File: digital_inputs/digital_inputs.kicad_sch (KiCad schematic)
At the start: 130 parts, among them J1 6437288-2, J10 Conn_01x01, J11 Conn_01x01, J12 Conn_01x01, J13 Conn_01x01, J14 Conn_01x01, J15 Conn_01x01, J16 Conn_01x01, J17 Conn_01x01, J19 6437288-3, J3 Conn_01x08, J4 Conn_01x01, J5 Conn_01x02, J6 Conn_01x04, J7 Conn_01x04, J8 Conn_01x04, J9 Conn_01x04, Q1 AO3400A, Q2 AO3400A, Q3 AO3400A, Q4 AO3400A, Q5 AO3400A, Q6 AO3400A, Q7 AO3400A, Q8 AO3400A, U1 OPA4192IPW, U10 ULN2003A, U11 NUCLEO-F429ZI, U12 TJA1051T-3, U2 CD4067BM96, U3 CD4067BM96, U4 CD4067BM96, U5 CD4067BM96, U6 CD4067BM96, U7 CD4067BM96, U8 TC4427, U9 TC4427

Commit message: Upd pcb
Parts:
- removed U11: NUCLEO-F429ZI, lib:MODULE_NUCLEO-F429ZI, symbol NUCLEO-F429ZI:NUCLEO-F429ZI
- added D2: PESD1CAN, Package_TO_SOT_SMD:SOT-23, symbol semiconductors:PESD1CAN
- added H1, H2, H3, H4, H5: MountingHole, MountingHole:MountingHole_3.2mm_M3, symbol Mechanical:MountingHole
- added J18: Conn_02x05_Odd_Even, Connector_PinHeader_2.54mm:PinHeader_2x05_P2.54mm_Vertical, symbol Connector_Generic:Conn_02x05_Odd_Even
- added J2: Conn_02x07_Odd_Even, Connector_PinHeader_2.54mm:PinHeader_2x07_P2.54mm_Vertical, symbol Connector_Generic:Conn_02x07_Odd_Even
- added J20: Conn_02x24_Odd_Even, Connector_PinHeader_2.54mm:PinHeader_2x24_P2.54mm_Vertical, symbol Connector_Generic:Conn_02x24_Odd_Even
- added J21: Conn_02x08_Odd_Even, Connector_PinHeader_2.54mm:PinHeader_2x08_P2.54mm_Vertical, symbol Connector_Generic:Conn_02x08_Odd_Even
- added J22: Conn_02x15_Odd_Even, Connector_PinHeader_2.54mm:PinHeader_2x15_P2.54mm_Vertical, symbol Connector_Generic:Conn_02x15_Odd_Even
- added J23, J25: Conn_02x10_Odd_Even, Connector_PinHeader_2.54mm:PinHeader_2x10_P2.54mm_Vertical, symbol Connector_Generic:Conn_02x10_Odd_Even
- added J24: Conn_02x17_Odd_Even, Connector_PinHeader_2.54mm:PinHeader_2x17_P2.54mm_Vertical, symbol Connector_Generic:Conn_02x17_Odd_Even
- added J26: Conn_02x06_Odd_Even, Connector_PinHeader_2.54mm:PinHeader_2x06_P2.54mm_Vertical, symbol Connector_Generic:Conn_02x06_Odd_Even
- added J27: Conn_02x16_Odd_Even, Connector_PinHeader_2.54mm:PinHeader_2x16_P2.54mm_Vertical, symbol Connector_Generic:Conn_02x16_Odd_Even
- added J28: Conn_02x04_Odd_Even, Connector_PinHeader_2.54mm:PinHeader_2x04_P2.54mm_Vertical, symbol Connector_Generic:Conn_02x04_Odd_Even
- added R56: DNP, Resistor_SMD:R_0402_1005Metric, symbol hellen1-wbo-rescue:R-Device
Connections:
- net +12V: now also J18.10 (Pin_10)
- net +5V: now also J18.4 (Pin_4)
- net ADR0: now also J25.2 (Pin_2)
- net ADR1: now also J25.4 (Pin_4)
- net ADR2: now also J25.6 (Pin_6)
- net ADR3: now also J25.13 (Pin_13)
- net CAN_H: now also D2.1 (G), R56.1
- net CAN_L: now also D2.2 (D), R56.2
- net CAN_RX: now also J25.14 (Pin_14)
- net CAN_TX: now also J25.12 (Pin_12)
- net GND: now also D2.3 (S), J18.5 (Pin_5), J18.6 (Pin_6), J18.8 (Pin_8), J2.8 (Pin_8), J20.25 (Pin_25), J20.36 (Pin_36), J20.47 (Pin_47), J20.48 (Pin_48), J21.11 (Pin_11), J21.13 (Pin_13), J22.12 (Pin_12), J22.23 (Pin_23), J23.8 (Pin_8), J24.17 (Pin_17), J24.22 (Pin_22), J24.27 (Pin_27), J24.3 (Pin_3), J24.5 (Pin_5), J25.20 (Pin_20), J25.9 (Pin_9), J26.12 (Pin_12), J27.22 (Pin_22), J27.31 (Pin_31), J27.7 (Pin_7), J28.7 (Pin_7), J28.8 (Pin_8)
- net IN0: now also J27.6 (Pin_6)
- net IN1: now also J27.4 (Pin_4)
- net IN2: now also J27.26 (Pin_26)
- net IN3: now also J27.10 (Pin_10)
- net MUX_OFF: now also J25.15 (Pin_15)
- net OUT0: now also J25.16 (Pin_16)
- net OUT1: now also J25.18 (Pin_18)
- net OUT2: now also J25.19 (Pin_19)
- net OUT3: now also J27.2 (Pin_2)
- net +3V3 renamed +3.3V
- net +3.3V: now also J18.2 (Pin_2)
- net HALL0_0 renamed DIG_0
- net DIG_0: now also J27.32 (Pin_32)
- net HALL0_1 renamed DIG_1
- net DIG_1: now also J27.12 (Pin_12)
- net HALL0_2 renamed DIG_2
- net DIG_2: now also J27.8 (Pin_8)
- net HALL0_3 renamed DIG_3
- net DIG_3: now also J27.20 (Pin_20)
- net HALL0_4 renamed DIG_4
- net DIG_4: now also J27.15 (Pin_15)
- net HALL0_5 renamed DIG_5
- net DIG_5: now also J27.24 (Pin_24)
- net HALL0_6 renamed DIG_6
- net DIG_6: now also J27.17 (Pin_17)
- net HALL0_7 renamed DIG_7
- net DIG_7: now also J27.23 (Pin_23)
- net OUT_HALL0_0 renamed OUT_DIG_0
- net OUT_HALL0_1 renamed OUT_DIG_1
- net OUT_HALL0_2 renamed OUT_DIG_2
- net OUT_HALL0_3 renamed OUT_DIG_3
- net OUT_HALL0_4 renamed OUT_DIG_4
- net OUT_HALL0_5 renamed OUT_DIG_5
- net OUT_HALL0_6 renamed OUT_DIG_6
- net OUT_HALL0_7 renamed OUT_DIG_7
- no-connect marks 19 -> 220
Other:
- moved on the sheet: C11

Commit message: #14 #16 #23
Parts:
- R24, R30: value 910 -> 820; LCSC C23264 -> C23253
- R26, R32, R39, R49: value 470 -> 820; LCSC C23179 -> C23253
- R27: value 100 -> 120; LCSC C22775 -> C22787
- R28, R43, R54, R55: value 910 -> 470; LCSC C23264 -> C23179
- R29: value 330 -> 100
- R31: value 470 -> 220; LCSC C23179 -> C22962
- R34: value 100 -> 470; LCSC C22775 -> C23179
- R35: value 100 -> 220; LCSC C22775 -> C22962
- R36: value 330 -> 820; LCSC C23138 -> C23253
- R37, R58: value 330 -> 510; LCSC C23138 -> C23193
- R38: value 910 -> 510; LCSC C23264 -> C23193
- R42: value 330 -> 220; LCSC C23138 -> C22962
- R53: value 470 -> 330; LCSC C23179 -> C23138
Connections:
- net 5V_2: now also R38.1; no longer R39.1
- net GND: now also R39.2; no longer R38.2
- net REF12: now also R38.2, R39.1; no longer R38.1, R39.2
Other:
- note added: "0.6V"
- note added: "0.8V"
- note added: "1.1V"
- note added: "1.4V"
- note added: "1.6V"
- note added: "1.9V"
- note added: "3.1V"
- note added: "3.4V"
- note removed: "1.2V"
- note removed: "1.3V"
- note removed: "1.7V"
- note removed: "3.3V"
- note removed: "3.7V"

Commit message: check
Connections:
- net 5V_2: now also R39.1; no longer R38.1
- net GND: now also R38.1; no longer R39.2
- net REF12: now also R39.2; no longer R39.1
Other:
- moved on the sheet: R38, R39
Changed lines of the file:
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@@
     (stroke (width 0) (type default))
   )
-  (wire (pts (xy 127 356.87) (xy 127 335.28))
+  (wire (pts (xy 127 335.28) (xy 127 356.87))
     (stroke (width 0) (type default))
   )
@@
     )
   )
-  (symbol (lib_id "Device:R") (at 130.81 340.36 0) (unit 1)
-    (in_bom yes) (on_board yes) (dnp no)
-    (property "Reference" "R39" (at 134.62 339.725 0)
-      (effects (font (size 1.27 1.27)))
-    )
-    (property "Value" "820" (at 134.62 341.63 0)
-      (effects (font (size 1.27 1.27)))
-    )
-    (property "Footprint" "Resistor_SMD:R_0603_1608Metric" (at 129.032 340.36 90)
-      (effects (font (size 1.27 1.27)) hide)
-    )
-    (property "Datasheet" "~" (at 130.81 340.36 0)
-      (effects (font (size 1.27 1.27)) hide)
-    )
-    (property "LCSC" "C23253" (at 130.81 340.36 0)
+  (symbol (lib_id "Device:R") (at 130.81 330.835 0) (unit 1)
+    (in_bom yes) (on_board yes) (dnp no)
+    (property "Reference" "R39" (at 134.62 330.2 0)
+      (effects (font (size 1.27 1.27)))
+    )
+    (property "Value" "820" (at 134.62 332.105 0)
+      (effects (font (size 1.27 1.27)))
+    )
+    (property "Footprint" "Resistor_SMD:R_0603_1608Metric" (at 129.032 330.835 90)
+      (effects (font (size 1.27 1.27)) hide)
+    )
+    (property "Datasheet" "~" (at 130.81 330.835 0)
+      (effects (font (size 1.27 1.27)) hide)
+    )
+    (property "LCSC" "C23253" (at 130.81 330.835 0)
       (effects (font (size 1.27 1.27)) hide)
     )
@@
     )
   )
-  (symbol (lib_id "Device:R") (at 130.81 330.835 0) (unit 1)
-    (in_bom yes) (on_board yes) (dnp no)
-    (property "Reference" "R38" (at 134.62 330.2 0)
-      (effects (font (size 1.27 1.27)))
-    )
-    (property "Value" "510" (at 134.62 332.105 0)
-      (effects (font (size 1.27 1.27)))
-    )
-    (property "Footprint" "Resistor_SMD:R_0603_1608Metric" (at 129.032 330.835 90)
-      (effects (font (size 1.27 1.27)) hide)
-    )
-    (property "Datasheet" "~" (at 130.81 330.835 0)
-      (effects (font (size 1.27 1.27)) hide)
-    )
-    (property "LCSC" "C23193" (at 130.81 330.835 0)
-      (effects (font (size 1.27 1.27)) hide)
-    )
+  (symbol (lib_id "Device:R") (at 130.81 340.36 180) (unit 1)
+    (in_bom yes) (on_board yes) (dnp no)
+    (property "Reference" "R38" (at 134.62 340.995 0)
+      (effects (font (size 1.27 1.27)))
+    )
+    (property "Value" "510" (at 134.62 339.09 0)
+      (effects (font (size 1.27 1.27)))
+    )
+    (property "Footprint" "Resistor_SMD:R_0603_1608Metric" (at 132.588 340.36 90)
+      (effects (font (size 1.27 1.27)) hide)
+    )
+    (property "Datasheet" "~" (at 130.81 340.36 0)
+      (effects (font (size 1.27 1.27)) hide)
+    )
+    (property "LCSC" "C23193" (at 130.81 340.36 0)
+      (effects (font (size 1.27 1.27)) hide)
+    )

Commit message: JLCPCB Part #
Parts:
- R29, R44, R46, R47, R59: LCSC C23138 -> C22775
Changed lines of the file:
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@@
       (effects (font (size 1.27 1.27)) hide)
     )
-    (property "LCSC" "C23138" (at 161.29 330.835 0)
+    (property "LCSC" "C22775" (at 161.29 330.835 0)
       (effects (font (size 1.27 1.27)) hide)
     )
@@
       (effects (font (size 1.27 1.27)) hide)
     )
-    (property "LCSC" "C23138" (at 151.765 330.835 0)
+    (property "LCSC" "C22775" (at 151.765 330.835 0)
       (effects (font (size 1.27 1.27)) hide)
     )
@@
       (effects (font (size 1.27 1.27)) hide)
     )
-    (property "LCSC" "C23138" (at 309.245 323.215 0)
+    (property "LCSC" "C22775" (at 309.245 323.215 0)
       (effects (font (size 1.27 1.27)) hide)
     )
@@
       (effects (font (size 1.27 1.27)) hide)
     )
-    (property "LCSC" "C23138" (at 299.72 323.215 0)
+    (property "LCSC" "C22775" (at 299.72 323.215 0)
       (effects (font (size 1.27 1.27)) hide)
     )
@@
       (effects (font (size 1.27 1.27)) hide)
     )
-    (property "LCSC" "C23138" (at 118.745 330.835 0)
+    (property "LCSC" "C22775" (at 118.745 330.835 0)
       (effects (font (size 1.27 1.27)) hide)
     )

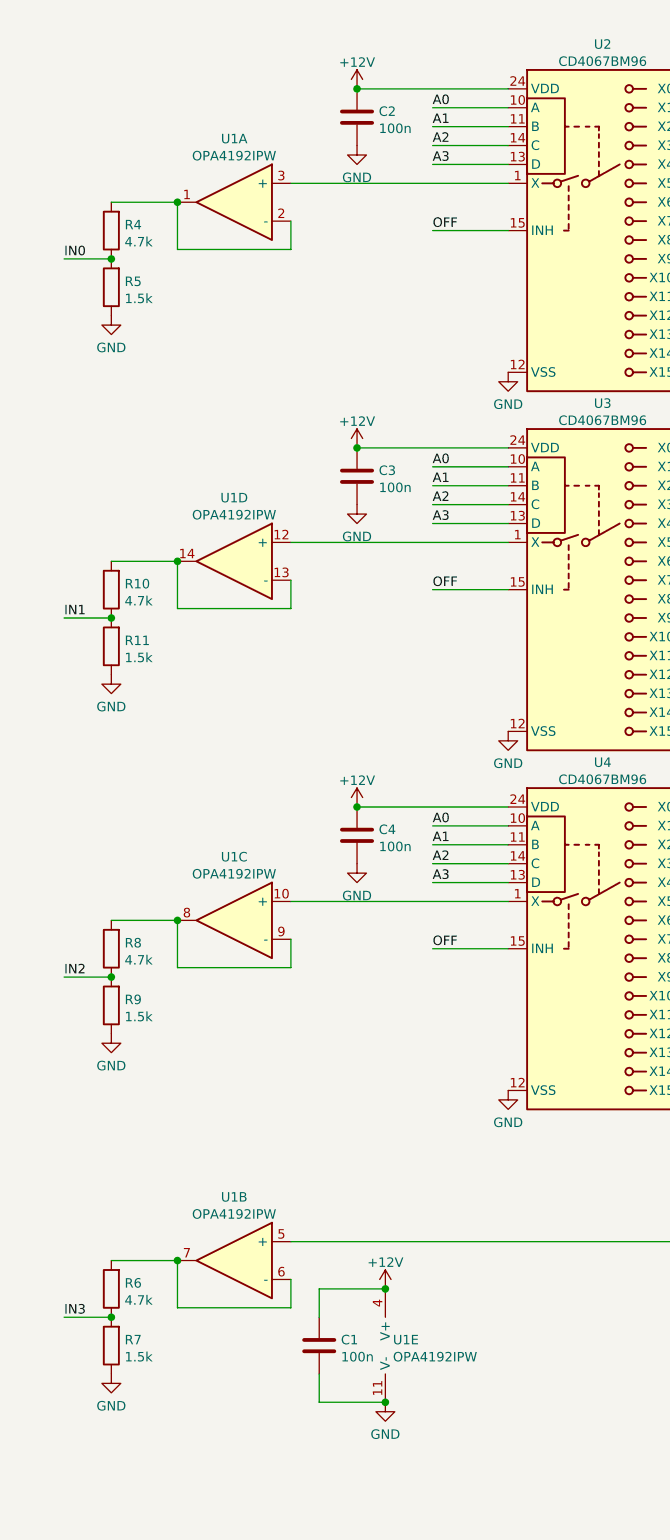
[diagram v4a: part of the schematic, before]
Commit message: Replace opamp
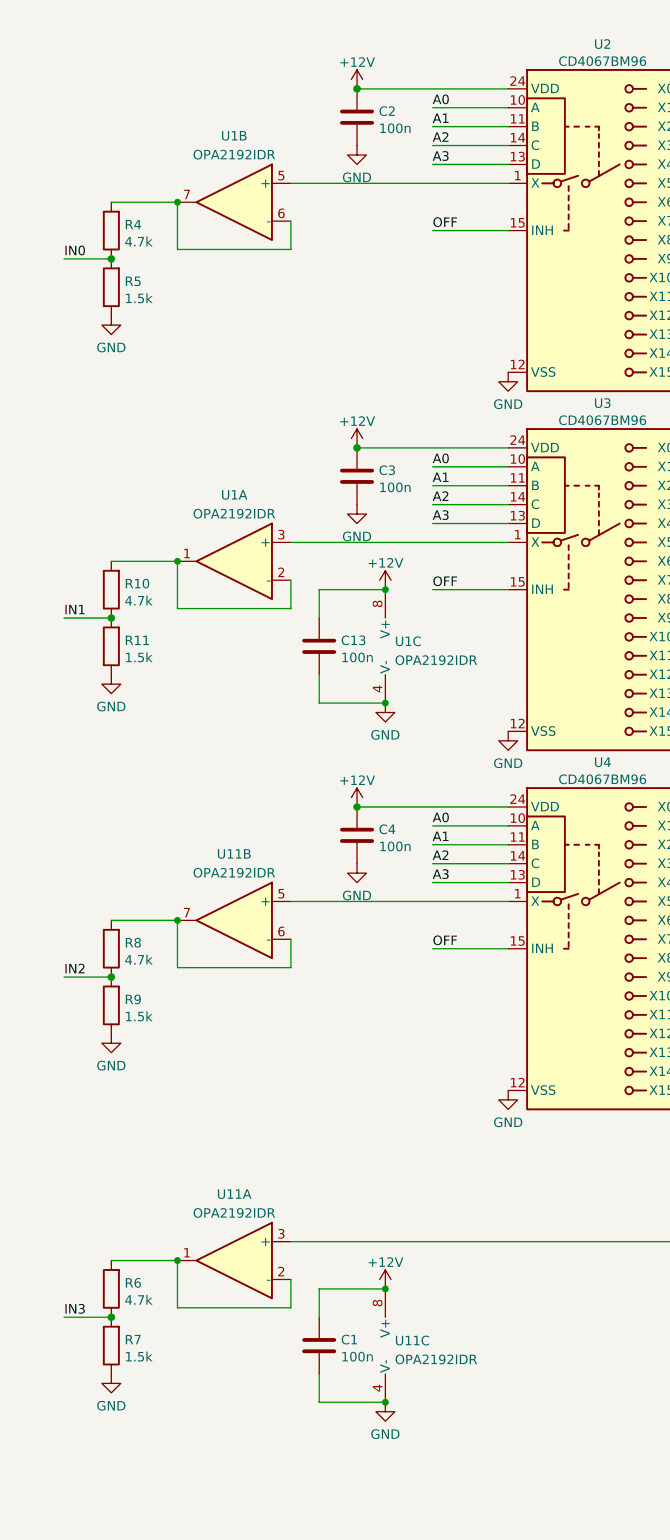
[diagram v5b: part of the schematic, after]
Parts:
- removed U1: OPA4192IPW, Package_SO:TSSOP-14_4.4x5mm_P0.65mm, symbol Amplifier_Operational:OPA4197xPW
- added C13: 100n, Capacitor_SMD:C_0603_1608Metric, symbol Device:C
- added U1, U11: OPA2192IDR, Package_SO:SO-8_3.9x4.9mm_P1.27mm, symbol Amplifier_Operational:OPA2134
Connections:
- net +12V: now also C13.2, U1.8 (V+), U11.8 (V+)
- net GND: now also C13.1, U1.4 (V-), U11.4 (V-)
- net TST49: now also U11.3 (+)
- net at R6.2: now also U11.1, U11.2 (-)
- net at R8.2: now also U11.6 (-), U11.7
- net at U4.1 (X): now also U11.5 (+)
- net at U3.1 (X): now also U1.3 (+)
- net at R4.2: now also U1.6 (-), U1.7
- net at U2.1 (X): now also U1.5 (+)
- net at R10.2: now also U1.1, U1.2 (-)

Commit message: #31 #26 #32 #33 #30
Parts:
- added D3, D4: LED-RED-0603, hellen-one-common:LED-0603, symbol hellen-one-common:LED_0603
- added R57, R60: 4.7k, Resistor_SMD:R_0603_1608Metric, symbol Device:R
- R13: value 4.7k -> 13k; LCSC C23162 -> C22797
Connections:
- net 5V_1: now also D3.1 (A)
- net 5V_2: now also D4.1 (A)
- net CAN_RX: now also J20.35 (Pin_35); no longer J25.14 (Pin_14)
- net CAN_TX: now also J20.33 (Pin_33); no longer J25.12 (Pin_12)
- net GND: now also R57.1, R60.1
- new net: D4.2 (K), R57.2
- new net: D3.2 (K), R60.2

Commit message: #29 #39 #40
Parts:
- added P1, P10, P11, P12, P13, P14, P15, P16, P17, P2, P3, P4, P5, P6, P7, P8, P9: Pad, hellen-one-common:PAD-TH, symbol hellen-one-common:Pad
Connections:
- net GND: now also J19.34 (34A), J19.38 (4B)
- net at J1.31 (31C): now also P14.1 (Pin_1)
- net at J1.32 (32C): now also P15.1 (Pin_1)
- net at J1.33 (33C): now also P16.1 (Pin_1)
- net at J1.34 (34C): now also P17.1 (Pin_1)
- net at J19.21 (21A): now also P1.1 (Pin_1)
- net at J19.22 (22A): now also P2.1 (Pin_1)
- net at J19.23 (23A): now also P3.1 (Pin_1)
- net at J19.24 (24A): now also P4.1 (Pin_1)
- net at J19.25 (25A): now also P5.1 (Pin_1)
- net at J19.26 (26A): now also P6.1 (Pin_1)
- net at J19.27 (27A): now also P7.1 (Pin_1)
- net at J19.28 (28A): now also P8.1 (Pin_1)
- net at J19.29 (29A): now also P9.1 (Pin_1)
- net at J19.30 (30A): now also P10.1 (Pin_1)
- net at J19.31 (31A): now also P11.1 (Pin_1)
- net at J19.32 (32A): now also P12.1 (Pin_1)
- net at J19.33 (33A): now also P13.1 (Pin_1)
- no-connect marks 220 -> 201
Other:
- moved on the sheet: F2, F3, F4, F5, F6, F7, F8, F9, H1, H2, H3, H4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

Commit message: Upd SCH
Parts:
- added C14, C15: 47p, Capacitor_SMD:C_0603_1608Metric, symbol hellen-one-common:Cap
- added C16: 100n, Capacitor_SMD:C_0603_1608Metric, symbol hellen-one-common:Cap
- added CB1: CircuitBreaker_1P, Button_Switch_SMD:SW_Push_SPST_NO_Alps_SKRK, symbol Device:CircuitBreaker_1P
- added D5: BZV55C10, Diode_SMD:D_MiniMELF, symbol Diode:BZV55C10
- added D6: PESD1CAN, Package_TO_SOT_SMD:SOT-23, symbol semiconductors:PESD1CAN
- added P18, P19: Pad, hellen-one-common:PAD-TH, symbol hellen-one-common:Pad
- added Q9: PJM2319PSA, Package_TO_SOT_SMD:SOT-23, symbol Transistor_FET:Si2319CDS
- added R61: 13k, Resistor_SMD:R_0603_1608Metric, symbol Device:R
- added R62: DNP, Resistor_SMD:R_0402_1005Metric, symbol hellen1-wbo-rescue:R-Device
- added U13: TJA1051T-3, Package_SO:SOIC-8_3.9x4.9mm_P1.27mm, symbol Interface_CAN_LIN:TJA1051T-3
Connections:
- net +12V: now also Q9.3 (D); no longer F1.1
- net +3.3V: now also U13.5 (VIO)
- net +5V: now also C16.2, U13.3 (VCC)
- net CAN_RX: now also J20.33 (PD0); no longer J20.35 (PG0)
- net CAN_TX: now also J20.31 (PD1); no longer J20.33 (PD0)
- net GND: now also C14.2, C15.1, C16.1, D6.3 (S), R61.1, U13.2 (GND), U13.8 (S)
- net OUT0: now also J25.10 (PD8); no longer J25.16 (PB12)
- net CAN2_TX: now reaches J25.17 (PB6)
- net CAN2_TX: now also U13.1 (TXD)
- new net: CB1.2, D5.1 (K), F1.1, Q9.2 (S)
- new net: CB1.1, D5.2 (A), Q9.1 (G), R61.2
- new net CAN2_H: C14.1, D6.1 (G), P18.1 (Pin_1), R62.1, U13.7 (CANH)
- new net CAN2_L: C15.2, D6.2 (D), P19.1 (Pin_1), R62.2, U13.6 (CANL)
- new net CAN2_RX: J25.16 (PB12), U13.4 (RXD)
- no-connect marks 201 -> 199
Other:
- note added: "NUCLEO-F429ZI"
- note added: "Pins PA11/PA12 are used as USB on the Nucleo board"
- moved on the sheet: C10, C11, C12, D3, F1, F3, F4, F5, F6, F7, F8, F9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
